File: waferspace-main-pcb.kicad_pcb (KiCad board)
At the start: 4 copper layers, 84 x 78 mm, 272 parts, among them J1 Conn_01x03, J10 Conn_01x02, J11 Conn_01x06, J12 Conn_01x03, J13 613012243121, J14 Conn_01x03, J17 Conn_01x03, J2 Conn_01x03, J20 USB_C, J3 613012243121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

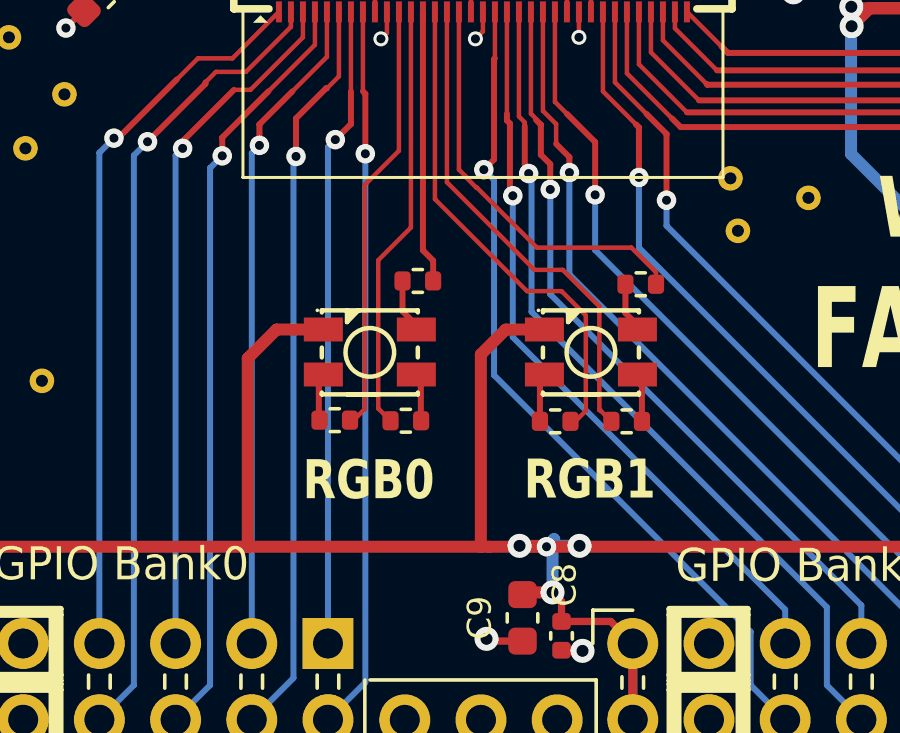
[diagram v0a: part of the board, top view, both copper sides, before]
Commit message: Fix RGB LEDs
Signed-off-by: Leo Moser <leomoser99@gmail.com>
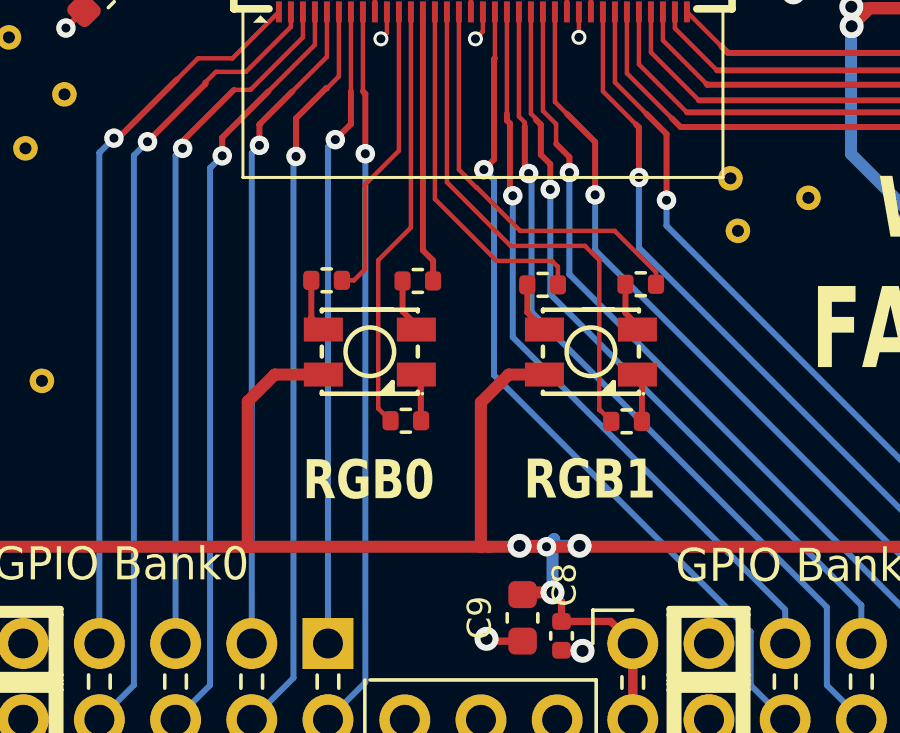
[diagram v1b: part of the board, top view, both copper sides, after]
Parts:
- moved R28 4.67 mm to (111.8, 114.3)
- moved R26 4.57 mm to (119.0, 114.5)
- turned D3 to 0 degrees
- turned D4 to 0 degrees
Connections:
- D3 pad 1: +3V3 -> Net-(D3-RK)
- D3 pad 2: Net-(D3-RK) -> +3V3
- D4 pad 1: +3V3 -> Net-(D4-RK)
- D4 pad 2: Net-(D4-RK) -> +3V3
- R25 pad 2: Net-(D4-RK) -> Net-(D4-GK)
- R26 pad 2: Net-(D4-GK) -> Net-(D4-BK)
- R27 pad 2: Net-(D4-BK) -> Net-(D4-RK)
- R28 pad 2: Net-(D3-GK) -> Net-(D3-BK)
- R29 pad 2: Net-(D3-RK) -> Net-(D3-GK)
- R30 pad 2: Net-(D3-BK) -> Net-(D3-RK)
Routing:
- net /fpga_pad[17]: track 16.7 -> 11.9 mm
- net /fpga_pad[14]: track 14.4 -> 9.97 mm
- net +3V3: track 636.6 -> 633.9 mm
- net /fpga_pad[18]: track 16.5 -> 17.4 mm
